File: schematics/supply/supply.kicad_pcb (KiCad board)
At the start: 4 copper layers, 110 x 175 mm, 224 parts, among them J1 Conn_01x02_Pin, J10 USBASP, J11 USBASP, J12 Conn_01x06_Pin, J14 banana jack + fuse 15A, J15 banana jack + fuse 15A, J16 Conn_02x04_Odd_Even, J17 jst xh angle, J18 jst xh angle, J2 Conn_01x01_Pin, J3 USB_A, J4 USB_A, J5 USB_A, J6 Conn_01x04_Pin, J8 Conn_01x04_Pin, M1 Fan, Q1 40N06, Q10 IRLML0030, Q11 IRLML5203, Q12 IRLML5203, Q2 STP13NK60Z, Q3 STP13NK60Z, Q4 IRLML0030, Q5 IRLML5203, Q6 IRLML5203, Q7 IRLML0030, Q8 IRLML0030, Q9 IRLML0030, SW3 SW_Push, U1 INA3221, U10 LM158DR, U11 LM1085-3.3, U12 ATmega328-A, U13 ATtiny1616-M, U15 LM158DR, U16 EL817, U17 IRS2153S, U18 TL331, U19 INA169, U2 EL817, U20 INA3221, U3 MC34063AD, U4 L78L33ACUTR, U5 IRS2153S, U6 LM158DR, U7 IP2163, U8 LM158DR, U9 TL432DBZ, X1 HC-49U, 16MHz, X2 CSX-750FCC, 16MHz

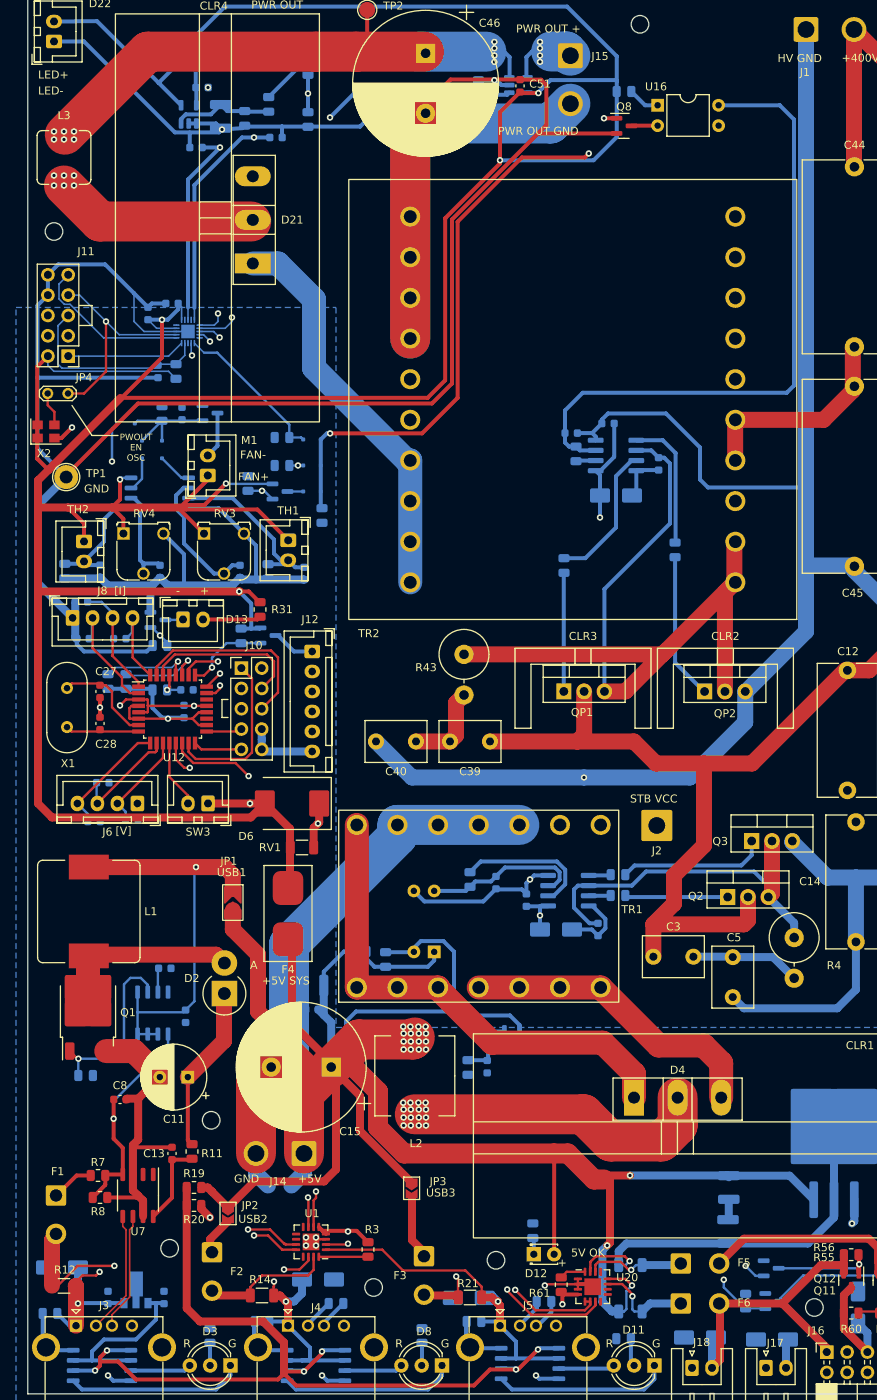
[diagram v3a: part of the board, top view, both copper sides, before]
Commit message: Added Li-Ion charger port
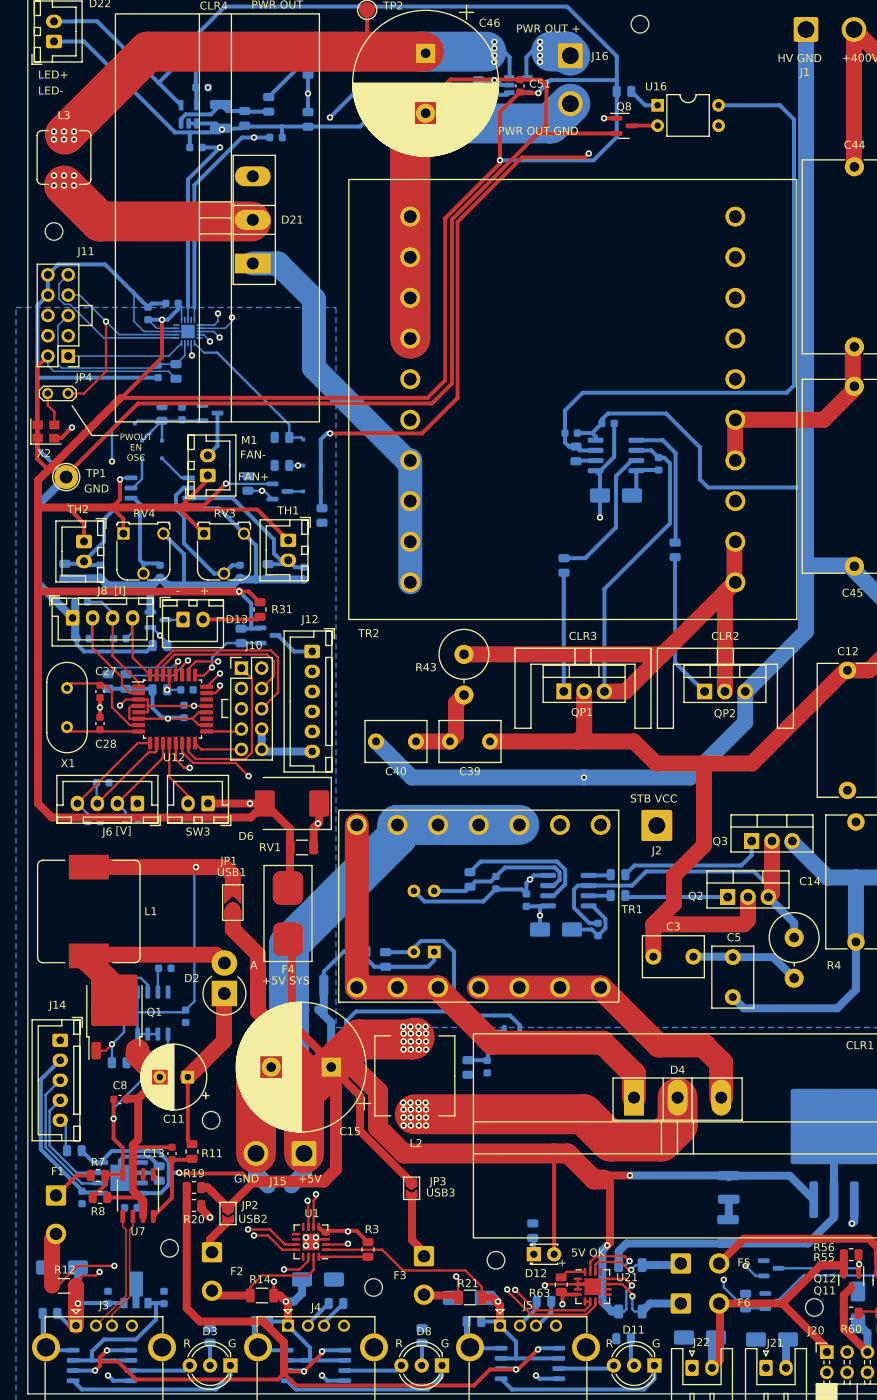
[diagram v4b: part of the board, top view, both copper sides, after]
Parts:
- added C52: 10 uF, Capacitor_SMD:C_0603_1608Metric, B.Cu at (99.3, 212.6)
- added C53: 10 uF, Capacitor_SMD:C_0603_1608Metric, B.Cu at (93.2, 211.2)
- added J14: Conn_01x05_Pin, Connector_JST:JST_XH_B5B-XH-A_1x05_P2.50mm_Vertical, F.Cu at (90.5, 191.6)
- added R61: 1K, Resistor_SMD:R_0805_2012Metric, B.Cu at (102.9, 208.2)
- added R62: 2K, Resistor_SMD:R_0805_2012Metric, B.Cu at (92.3, 205.4)
- added U20: TP4056, Library:SOP127P600X175-9N, B.Cu at (98.0, 208.8)
- moved R6 4.49 mm to (97.9, 194.4)
- moved Q1 3.30 mm to (97.3, 187.9)
- renumbered J14 to J15, J15 to J16, J16 to J20, J17 to J21, J18 to J22, R61 to R63, U20 to U21
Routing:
- net /Internal 5V & out usb/+5V_OUT: track 312.9 -> 345.6 mm, vias 19 -> 20
- net /Output connectors/LIION_CHARGE_VBAT: track 0.00 -> 21.7 mm
- net /Output connectors/LIION_CHARGE_LED2: track 0.00 -> 17.8 mm
- net /Output connectors/LIION_CHARGE_LED1: track 0.00 -> 13.9 mm
- net GND: track 929.6 -> 935.6 mm
- net Net-(Q1-G): track 22.7 -> 17.3 mm
- net Net-(J14-Pin_5): track 0.00 -> 3.64 mm
- net Net-(U20-ISET): track 0.00 -> 2.84 mm
- net Net-(D2-A): track 21.9 -> 23.2 mm

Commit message: Boards prepared to order
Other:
- board text added: "0,0000 mm / 0,0000 mm"
- board text added: "0,3000 mm"
- board text added: "1,6000 mm"
- board text added: "110,0000 mm x 175,0000 mm"
- board text added: "4"
- board text added: "None"
- board text added: "Габариты платы:"
- board text added: "Количество слоёв меди:"
- board text added: "Контроль импеданса:"
- board text added: "Краевой соединитель:"
- board text added: "Метал. торцы:"
- board text added: "Мин. дорожка/зазор:"
- board text added: "Мин. сверло:"
- board text added: "Нет"
- board text added: "Периферийные полу-отверстия:"
- board text added: "Покрытие меди:"
- board text added: "Толщина платы:"
- board text added: "ХАРАКТЕРИСТИКИ ПЛАТЫ"
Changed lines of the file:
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@@
     (fp_line (start 12.45 3.4) (end 12.45 -2.35)
       (stroke (width 0.1) (type solid)) (layer "F.Fab"))
-    (pad "1" thru_hole roundrect (at 0 0 270) (size 1.7 1.95) (drill 0.95) (layers "*.Cu" "*.Mask") (roundrect_rratio 0.147059)
+    (pad "1" thru_hole roundrect (at 0 0 270) (size 1.7 1.95) (drill 0.95) (layers "*.Cu" "*.Mask") (roundrect_rratio 0.1470588235)
       (net 2 "GND") (pinfunction "Pin_1") (pintype "passive"))
     (pad "2" thru_hole oval (at 2.5 0 270) (size 1.7 1.95) (drill 0.95) (layers "*.Cu" "*.Mask")
@@
     (fp_line (start 1 0.625) (end 1 -0.625)
       (stroke (width 0.1) (type solid)) (layer "B.Fab"))
-    (pad "1" smd roundrect (at -0.9125 0 270) (size 1.025 1.4) (layers "B.Cu" "B.Paste" "B.Mask") (roundrect_rratio 0.243902)
+    (pad "1" smd roundrect (at -0.9125 0 270) (size 1.025 1.4) (layers "B.Cu" "B.Paste" "B.Mask") (roundrect_rratio 0.243902439)
       (net 2 "GND") (pintype "passive"))
-    (pad "2" smd roundrect (at 0.9125 0 270) (size 1.025 1.4) (layers "B.Cu" "B.Paste" "B.Mask") (roundrect_rratio 0.243902)
+    (pad "2" smd roundrect (at 0.9125 0 270) (size 1.025 1.4) (layers "B.Cu" "B.Paste" "B.Mask") (roundrect_rratio 0.243902439)
       (net 150 "Net-(U20-ISET)") (pintype "passive"))
     (model "${KICAD6_3DMODEL_DIR}/Resistor_SMD.3dshapes/R_0805_2012Metric.wrl"
@@
     (fp_line (start 1 0.625) (end 1 -0.625)
       (stroke (width 0.1) (type solid)) (layer "B.Fab"))
-    (pad "1" smd roundrect (at -0.9125 0 180) (size 1.025 1.4) (layers "B.Cu" "B.Paste" "B.Mask") (roundrect_rratio 0.243902)
+    (pad "1" smd roundrect (at -0.9125 0 180) (size 1.025 1.4) (layers "B.Cu" "B.Paste" "B.Mask") (roundrect_rratio 0.243902439)
       (net 42 "/Internal 5V & out usb/+5V_OUT") (pintype "passive"))
-    (pad "2" smd roundrect (at 0.9125 0 180) (size 1.025 1.4) (layers "B.Cu" "B.Paste" "B.Mask") (roundrect_rratio 0.243902)
+    (pad "2" smd roundrect (at 0.9125 0 180) (size 1.025 1.4) (layers "B.Cu" "B.Paste" "B.Mask") (roundrect_rratio 0.243902439)
       (net 149 "Net-(J14-Pin_5)") (pintype "passive"))
     (model "${KICAD6_3DMODEL_DIR}/Resistor_SMD.3dshapes/R_0805_2012Metric.wrl"
@@
     (effects (font (size 1 1) (thickness 0.15)) (justify left bottom))
   )
+  (gr_text "Толщина платы: " (at 349.021421 25.394) (layer "User.1")
+    (effects (font (size 1.5 1.5) (thickness 0.2)) (justify left top))
+  )
+  (gr_text "4" (at 312.007141 25.394) (layer "User.1")
+    (effects (font (size 1.5 1.5) (thickness 0.2)) (justify left top))
+  )
+  (gr_text "Количество слоёв меди: " (at 271.85 25.394) (layer "User.1")
+    (effects (font (size 1.5 1.5) (thickness 0.2)) (justify left top))
+  )
+  (gr_text "Периферийные полу-отверстия: " (at 271.85 41.222) (layer "User.1")
+    (effects (font (size 1.5 1.5) (thickness 0.2)) (justify left top))
+  )
+  (gr_text "Мин. дорожка/зазор: " (at 271.85 33.308) (layer "User.1")
+    (effects (font (size 1.5 1.5) (thickness 0.2)) (justify left top))
+  )
+  (gr_text "Габариты платы: " (at 271.85 29.351) (layer "User.1")
+    (effects (font (size 1.5 1.5) (thickness 0.2)) (justify left top))
+  )
+  (gr_text "Мин. сверло: " (at 349.021421 33.308) (layer "User.1")
+    (effects (font (size 1.5 1.5) (thickness 0.2)) (justify left top))
+  )
+  (gr_text "Нет" (at 376.607136 37.265) (layer "User.1")
+    (effects (font (size 1.5 1.5) (thickness 0.2)) (justify left top))
+  )
+  (gr_text "Контроль импеданса: " (at 349.021421 37.265) (layer "User.1")
+    (effects (font (size 1.5 1.5) (thickness 0.2)) (justify left top))
+  )
+  (gr_text "110,0000 mm x 175,0000 mm" (at 312.007141 29.351) (layer "User.1")
+    (effects (font (size 1.5 1.5) (thickness 0.2)) (justify left top))
+  )
+  (gr_text "None" (at 312.007141 37.265) (layer "User.1")
+    (effects (font (size 1.5 1.5) (thickness 0.2)) (justify left top))
+  )
+  (gr_text "Нет" (at 376.607136 41.222) (layer "User.1")
+    (effects (font (size 1.5 1.5) (thickness 0.2)) (justify left top))
+  )
+  (gr_text "Нет" (at 312.007141 45.179) (layer "User.1")
+    (effects (font (size 1.5 1.5) (thickness 0.2)) (justify left top))
+  )
+  (gr_text "" (at 349.021421 29.351) (layer "User.1")
+    (effects (font (size 1.5 1.5) (thickness 0.2)) (justify left top))
+  )
+  (gr_text "Покрытие меди: " (at 271.85 37.265) (layer "User.1")
+    (effects (font (size 1.5 1.5) (thickness 0.2)) (justify left top))
+  )
+  (gr_text "Нет" (at 312.007141 41.222) (layer "User.1")
+    (effects (font (size 1.5 1.5) (thickness 0.2)) (justify left top))
+  )
+  (gr_text "" (at 376.607136 29.351) (layer "User.1")
+    (effects (font (size 1.5 1.5) (thickness 0.2)) (justify left top))
+  )
+  (gr_text "0,3000 mm" (at 376.607136 33.308) (layer "User.1")
+    (effects (font (size 1.5 1.5) (thickness 0.2)) (justify left top))
+  )
+  (gr_text "1,6000 mm" (at 376.607136 25.394) (layer "User.1")
+    (effects (font (size 1.5 1.5) (thickness 0.2)) (justify left top))
+  )
+  (gr_text "0,0000 mm / 0,0000 mm" (at 312.007141 33.308) (layer "User.1")
+    (effects (font (size 1.5 1.5) (thickness 0.2)) (justify left top))
+  )
+  (gr_text "Краевой соединитель: " (at 271.85 45.179) (layer "User.1")
+    (effects (font (size 1.5 1.5) (thickness 0.2)) (justify left top))
+  )
+  (gr_text "ХАРАКТЕРИСТИКИ ПЛАТЫ" (at 271.1 19.9) (layer "User.1")
+    (effects (font (size 2 2) (thickness 0.4)) (justify left top))
+  )
+  (gr_text "Метал. торцы: " (at 349.021421 41.222) (layer "User.1")
+    (effects (font (size 1.5 1.5) (thickness 0.2)) (justify left top))
+  )
   (via (at 156 158.75) (size 0.8) (drill 0.4) (layers "F.Cu" "B.Cu") (net 1))
   (via (at 149.25 171.5) (size 0.8) (drill 0.4) (layers "F.Cu" "B.Cu") (net 1))
@@
     )
   )
+  (group "group-boardCharacteristics" (id b7c5549e-9abb-47fe-bdfb-868d471fbcc3)
+    (members
+      0bfab9ac-c7c6-4d77-9e8c-998ad8ed6424
+      1438afa5-2d04-4a34-b753-727b26259eb9
+      28fd517b-9697-4a94-a525-f6dac9960201
+      365f07fc-01e8-4f98-88f4-23c7a85ddfa1
+      485137ed-b0f4-4455-b13c-be568ca291c7
+      522984a3-1481-42bc-a8e9-0acb3c388a79
+      56f255be-c6be-4243-9d5d-7ae2e8d7bde8
+      659d1fc8-3387-498f-bab2-99843c33d28e
+      736ccc0e-d616-4e42-9bfb-46748ac58566
+      807211ef-b4ff-4a6b-9f62-d9aa4556b839
+      8b7a0ee2-2ee5-450a-b0b3-fc22ba2378d3
+      8caba954-9fd2-4507-866c-c7bee777b311
+      8cae5032-510a-4c70-9292-7fc84607ec86
+      97584542-618d-4a3a-ba2a-ca0d0623e70e
+      9ddd0f56-54ff-4b05-bf25-7ee60b267137
+      a226faaf-a7c1-4141-83ac-1c969bf0bfee
+      b28a6cec-5f06-4634-b74f-6f1b2c9f94ec
+      b29c0600-97ef-421b-9ddb-9213dd12ffad
+      bb301a07-bf95-4678-8b18-b7c7567b25d8
+      bf8efdb3-ac0b-457b-9789-3843c7a35fd9
+      c52c5261-a81b-4d71-8d20-c7d6050ea6fa
+      d38eff0f-d84b-450f-9e8d-778055bbda02
+      d50891c1-1e65-49d2-94ec-f2d8f67db00b
+    )
+  )
